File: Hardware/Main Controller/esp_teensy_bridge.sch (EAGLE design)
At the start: 64 parts, among them IC1 BQ79600PWRQ1, Q5 VISHAY_SIS862DN-T1-GE3VISHAY_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, Q6 VISHAY_SIS862DN-T1-GE3VISHAY_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, Q7 VISHAY_SIS862DN-T1-GE3VISHAY_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, Q8 VISHAY_SIS862DN-T1-GE3VISHAY_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, U1 MCP2562-E/SN, X1 5566-12

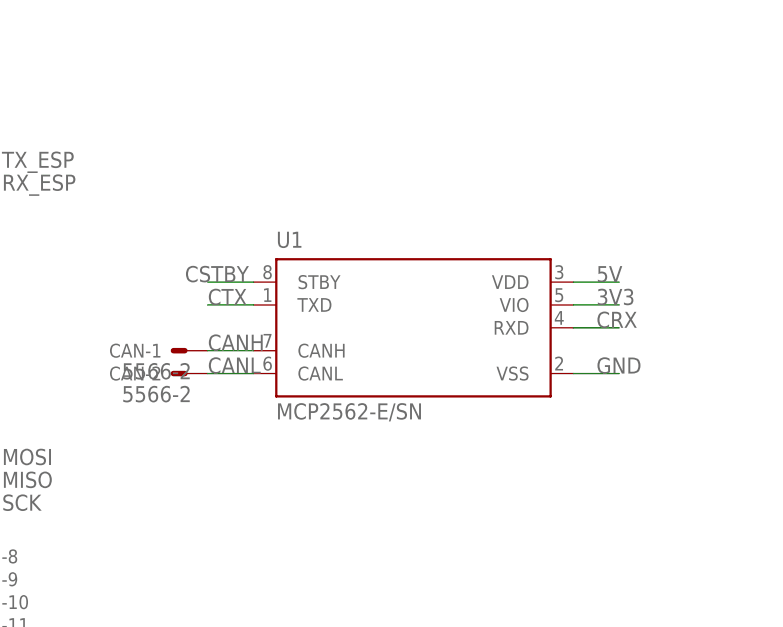
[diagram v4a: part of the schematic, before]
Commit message: Work on BQ library, RC fix for SR
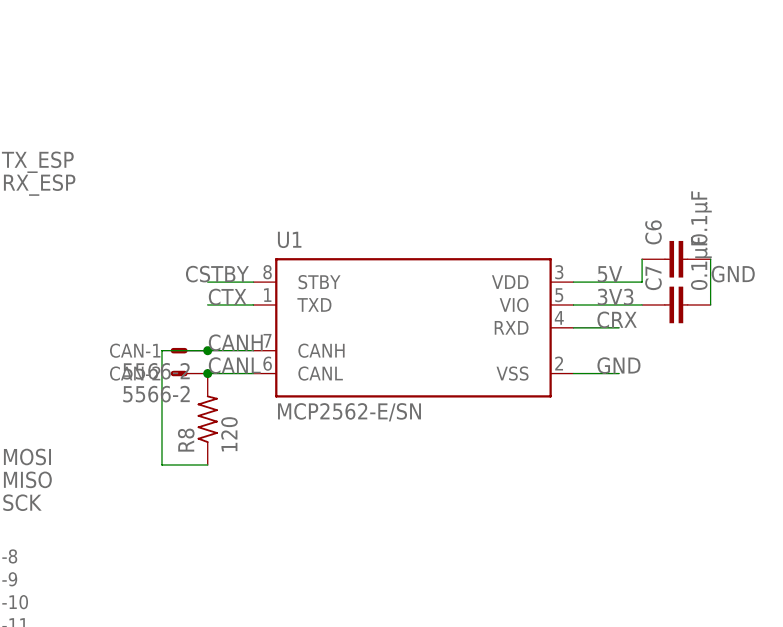
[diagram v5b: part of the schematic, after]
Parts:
- added C6, C7: 0.1μF, rcl:C-EUC0603
- added R8: 120, rcl:R-US_R0603
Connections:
- net 3V3: now also C7.1
- net 5V: now also C6.1
- net CANH: now also R8.1
- net CANL: now also R8.2
- net GND: now also C6.2, C7.2
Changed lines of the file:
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@@
 <part name="U1" library="MCP2562-E_SN" deviceset="MCP2562-E/SN" device=""/>
 <part name="CAN" library="con-molex" library_urn="urn:adsk.eagle:library:165" deviceset="5566-2" device="" package3d_urn="urn:adsk.eagle:package:8078583/1"/>
+<part name="C6" library="rcl" library_urn="urn:adsk.eagle:library:334" deviceset="C-EU" device="C0603" package3d_urn="urn:adsk.eagle:package:23616/2" value="0.1μF"/>
+<part name="C7" library="rcl" library_urn="urn:adsk.eagle:library:334" deviceset="C-EU" device="C0603" package3d_urn="urn:adsk.eagle:package:23616/2" value="0.1μF"/>
+<part name="R8" library="rcl" library_urn="urn:adsk.eagle:library:334" deviceset="R-US_" device="R0603" package3d_urn="urn:adsk.eagle:package:23555/3" value="120"/>
 </parts>
 <sheets>
@@
 <attribute name="NAME" x="124.46" y="79.502" size="1.524" layer="95" rot="R180"/>
 <attribute name="VALUE" x="127.762" y="77.343" size="1.778" layer="96" rot="R180"/>
+</instance>
+<instance part="C6" gate="G$1" x="180.34" y="91.44" smashed="yes" rot="R90">
+<attribute name="NAME" x="179.959" y="92.964" size="1.778" layer="95" rot="R90"/>
+<attribute name="VALUE" x="185.039" y="92.964" size="1.778" layer="96" rot="R90"/>
+</instance>
+<instance part="C7" gate="G$1" x="180.34" y="86.36" smashed="yes" rot="R90">
+<attribute name="NAME" x="179.959" y="87.884" size="1.778" layer="95" rot="R90"/>
+<attribute name="VALUE" x="185.039" y="87.884" size="1.778" layer="96" rot="R90"/>
+</instance>
+<instance part="R8" gate="G$1" x="129.54" y="73.66" smashed="yes" rot="R90">
+<attribute name="NAME" x="128.0414" y="69.85" size="1.778" layer="95" rot="R90"/>
+<attribute name="VALUE" x="132.842" y="69.85" size="1.778" layer="96" rot="R90"/>
 </instance>
 </instances>
@@
 <label x="172.72" y="78.74" size="1.778" layer="95"/>
 </segment>
+<segment>
+<pinref part="C6" gate="G$1" pin="2"/>
+<pinref part="C7" gate="G$1" pin="2"/>
+<wire x1="185.42" y1="91.44" x2="185.42" y2="86.36" width="0.1524" layer="91"/>
+<label x="185.42" y="88.9" size="1.778" layer="95"/>
+</segment>
 </net>
 <net name="N$1" class="0">
@@
 <segment>
 <pinref part="U1" gate="G$1" pin="VDD"/>
-<wire x1="170.18" y1="88.9" x2="175.26" y2="88.9" width="0.1524" layer="91"/>
+<wire x1="170.18" y1="88.9" x2="177.8" y2="88.9" width="0.1524" layer="91"/>
 <label x="172.72" y="88.9" size="1.778" layer="95"/>
+<pinref part="C6" gate="G$1" pin="1"/>
+<wire x1="177.8" y1="88.9" x2="177.8" y2="91.44" width="0.1524" layer="91"/>
 </segment>
 </net>
@@
 <segment>
 <pinref part="U1" gate="G$1" pin="VIO"/>
-<wire x1="170.18" y1="86.36" x2="175.26" y2="86.36" width="0.1524" layer="91"/>
+<wire x1="170.18" y1="86.36" x2="177.8" y2="86.36" width="0.1524" layer="91"/>
 <label x="172.72" y="86.36" size="1.778" layer="95"/>
+<pinref part="C7" gate="G$1" pin="1"/>
 </segment>
 </net>
@@
 <wire x1="134.62" y1="81.28" x2="129.54" y2="81.28" width="0.1524" layer="91"/>
 <label x="129.54" y="81.28" size="1.778" layer="95"/>
+<wire x1="129.54" y1="81.28" x2="124.46" y2="81.28" width="0.1524" layer="91"/>
+<wire x1="124.46" y1="81.28" x2="124.46" y2="68.58" width="0.1524" layer="91"/>
+<junction x="129.54" y="81.28"/>
+<pinref part="R8" gate="G$1" pin="1"/>
+<wire x1="124.46" y1="68.58" x2="129.54" y2="68.58" width="0.1524" layer="91"/>
 </segment>
 </net>
@@
 <wire x1="134.62" y1="78.74" x2="129.54" y2="78.74" width="0.1524" layer="91"/>
 <label x="129.54" y="78.74" size="1.778" layer="95"/>
-</segment>
-</net>
+<pinref part="R8" gate="G$1" pin="2"/>
+<junction x="129.54" y="78.74"/>
+</segment>
+</net>

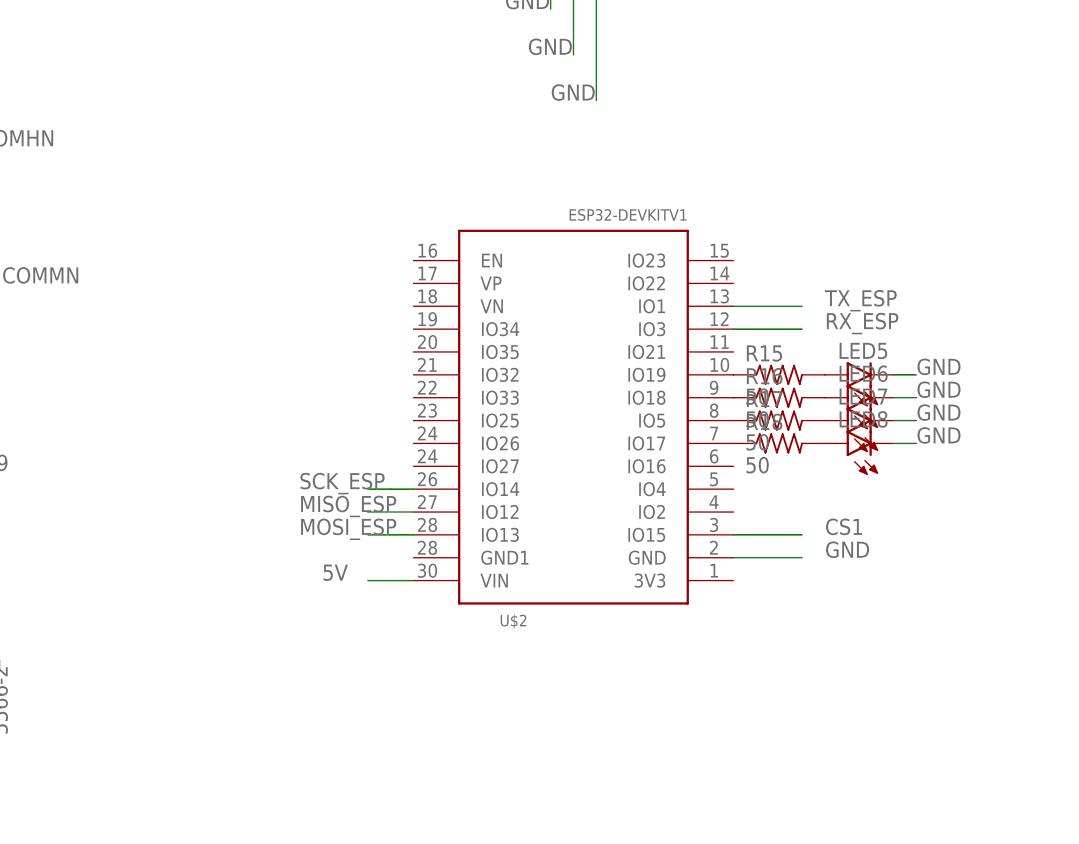
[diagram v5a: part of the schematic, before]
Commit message: ESP32-devkitc-32D instead ov DEVKIT V1
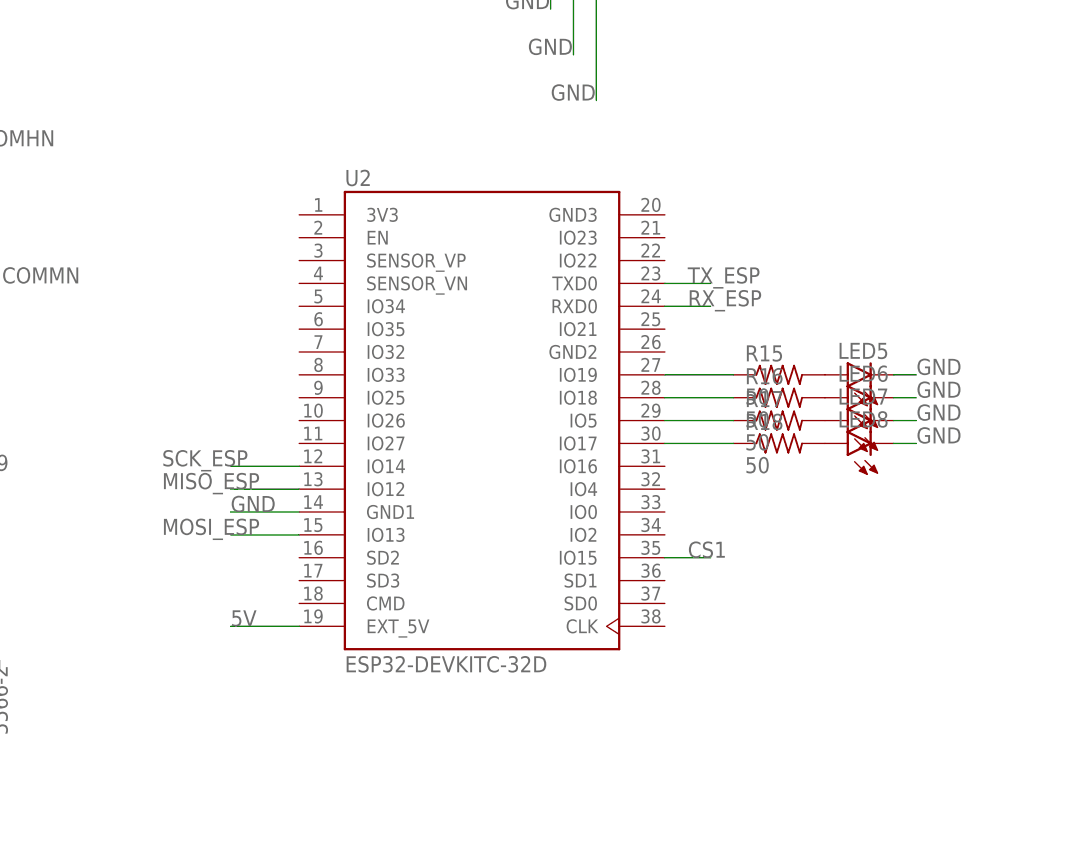
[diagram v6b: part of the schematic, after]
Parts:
- removed U$2: ESP32DEVKITV1, ESP32-DEVKITV1:ESP32DEVKITV1
- added U2: ESP32-DEVKITC-32D, ESP32-DEVKITC-32D:ESP32-DEVKITC-32D
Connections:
- net 5V: now also U2.EXT_5V; no longer U$2.VIN
- net CS1: now also U2.IO15; no longer U$2.IO15
- net GND: now also U2.GND1; no longer U$2.GND
- net MISO_ESP: now also U2.IO12; no longer U$2.IO12
- net MOSI_ESP: now also U2.IO13; no longer U$2.IO13
- net N$28: now also U2.IO19; no longer U$2.IO19
- net N$29: now also U2.IO18; no longer U$2.IO18
- net N$30: now also U2.IO5; no longer U$2.IO5
- net N$31: now also U2.IO17; no longer U$2.IO17
- net RX_ESP: now also U2.RXD0; no longer U$2.IO3
- net SCK_ESP: now also U2.IO14; no longer U$2.IO14
- net TX_ESP: now also U2.TXD0; no longer U$2.IO1
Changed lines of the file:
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@@
 <parts>
 <part name="IC1" library="BQ79600" deviceset="BQ79600PWRQ1" device=""/>
-<part name="U$2" library="ESP32-DEVKITV1" deviceset="ESP32DEVKITV1" device=""/>
 <part name="C1" library="rcl" library_urn="urn:adsk.eagle:library:334" deviceset="C-EU" device="C0603" package3d_urn="urn:adsk.eagle:package:23616/2" value="0.22μF"/>
 <part name="C2" library="rcl" library_urn="urn:adsk.eagle:library:334" deviceset="C-EU" device="C0603" package3d_urn="urn:adsk.eagle:package:23616/2" value="0.1μF"/>
@@
 <part name="C7" library="rcl" library_urn="urn:adsk.eagle:library:334" deviceset="C-EU" device="C0603" package3d_urn="urn:adsk.eagle:package:23616/2" value="0.1μF"/>
 <part name="R8" library="rcl" library_urn="urn:adsk.eagle:library:334" deviceset="R-US_" device="R0603" package3d_urn="urn:adsk.eagle:package:23555/3" value="120"/>
+<part name="U2" library="ESP32-DEVKITC-32D" deviceset="ESP32-DEVKITC-32D" device=""/>
 </parts>
 <sheets>
@@
 <attribute name="VALUE" x="-19.05" y="71.12" size="1.778" layer="96" align="center-left"/>
 </instance>
-<instance part="U$2" gate="G$1" x="63.5" y="-10.16" smashed="yes" rot="R90">
-<attribute name="NAME" x="58.42" y="-36.83" size="1.27" layer="95" rot="R180"/>
-</instance>
 <instance part="C1" gate="G$1" x="-68.58" y="66.04" smashed="yes" rot="R270">
 <attribute name="NAME" x="-68.199" y="64.516" size="1.778" layer="95" rot="R270"/>
@@
 <attribute name="NAME" x="128.0414" y="69.85" size="1.778" layer="95" rot="R90"/>
 <attribute name="VALUE" x="132.842" y="69.85" size="1.778" layer="96" rot="R90"/>
+</instance>
+<instance part="U2" gate="G$1" x="53.34" y="-15.24" smashed="yes">
+<attribute name="NAME" x="38.0828" y="10.8243" size="1.78" layer="95"/>
+<attribute name="VALUE" x="38.0837" y="-43.2098" size="1.7799" layer="96"/>
 </instance>
 </instances>
@@
 <wire x1="-15.24" y1="48.26" x2="-10.16" y2="48.26" width="0.1524" layer="91"/>
 <label x="-7.62" y="48.26" size="1.778" layer="95"/>
-</segment>
-<segment>
-<pinref part="U$2" gate="G$1" pin="GND"/>
-<wire x1="81.28" y1="-30.48" x2="88.9" y2="-30.48" width="0.1524" layer="91"/>
-<label x="91.44" y="-30.48" size="1.778" layer="95"/>
 </segment>
 <segment>
@@
 <label x="185.42" y="88.9" size="1.778" layer="95"/>
 </segment>
+<segment>
+<pinref part="U2" gate="G$1" pin="GND1"/>
+<wire x1="33.02" y1="-25.4" x2="25.4" y2="-25.4" width="0.1524" layer="91"/>
+<label x="25.4" y="-25.4" size="1.778" layer="95"/>
+</segment>
 </net>
 <net name="N$1" class="0">
@@
 </segment>
 <segment>
-<pinref part="U$2" gate="G$1" pin="IO1"/>
-<wire x1="81.28" y1="-2.54" x2="88.9" y2="-2.54" width="0.1524" layer="91"/>
-<label x="91.44" y="-2.54" size="1.778" layer="95"/>
+<pinref part="U2" gate="G$1" pin="TXD0"/>
+<wire x1="73.66" y1="0" x2="78.74" y2="0" width="0.1524" layer="91"/>
+<label x="76.2" y="0" size="1.778" layer="95"/>
 </segment>
 </net>
@@
 </segment>
 <segment>
-<pinref part="U$2" gate="G$1" pin="IO3"/>
-<wire x1="81.28" y1="-5.08" x2="88.9" y2="-5.08" width="0.1524" layer="91"/>
-<label x="91.44" y="-5.08" size="1.778" layer="95"/>
+<pinref part="U2" gate="G$1" pin="RXD0"/>
+<wire x1="73.66" y1="-2.54" x2="78.74" y2="-2.54" width="0.1524" layer="91"/>
+<label x="76.2" y="-2.54" size="1.778" layer="95"/>
 </segment>
 </net>
 <net name="5V" class="0">
-<segment>
-<pinref part="U$2" gate="G$1" pin="VIN"/>
-<wire x1="45.72" y1="-33.02" x2="40.64" y2="-33.02" width="0.1524" layer="91"/>
-<label x="35.56" y="-33.02" size="1.778" layer="95"/>
-</segment>
 <segment>
 <pinref part="TME1205S" gate="G$1" pin="+VOUT"/>
@@
 <pinref part="C6" gate="G$1" pin="1"/>
 <wire x1="177.8" y1="88.9" x2="177.8" y2="91.44" width="0.1524" layer="91"/>
+</segment>
+<segment>
+<pinref part="U2" gate="G$1" pin="EXT_5V"/>
+<wire x1="33.02" y1="-38.1" x2="25.4" y2="-38.1" width="0.1524" layer="91"/>
+<label x="25.4" y="-38.1" size="1.778" layer="95"/>
 </segment>
 </net>
@@
 </segment>
 <segment>
-<pinref part="U$2" gate="G$1" pin="IO15"/>
-<wire x1="81.28" y1="-27.94" x2="88.9" y2="-27.94" width="0.1524" layer="91"/>
-<label x="91.44" y="-27.94" size="1.778" layer="95"/>
+<pinref part="U2" gate="G$1" pin="IO15"/>
+<wire x1="73.66" y1="-30.48" x2="78.74" y2="-30.48" width="0.1524" layer="91"/>
+<label x="76.2" y="-30.48" size="1.778" layer="95"/>
 </segment>
 </net>
@@
 </segment>
 <segment>
-<pinref part="U$2" gate="G$1" pin="IO13"/>
-<wire x1="45.72" y1="-27.94" x2="40.64" y2="-27.94" width="0.1524" layer="91"/>
-<label x="33.02" y="-27.94" size="1.778" layer="95"/>
+<pinref part="U2" gate="G$1" pin="IO13"/>
+<wire x1="33.02" y1="-27.94" x2="25.4" y2="-27.94" width="0.1524" layer="91"/>
+<label x="17.78" y="-27.94" size="1.778" layer="95"/>
 </segment>
 </net>
@@
 </segment>
 <segment>
-<pinref part="U$2" gate="G$1" pin="IO12"/>
-<wire x1="45.72" y1="-25.4" x2="40.64" y2="-25.4" width="0.1524" layer="91"/>
-<label x="33.02" y="-25.4" size="1.778" layer="95"/>
+<pinref part="U2" gate="G$1" pin="IO12"/>
+<wire x1="33.02" y1="-22.86" x2="25.4" y2="-22.86" width="0.1524" layer="91"/>
+<label x="17.78" y="-22.86" size="1.778" layer="95"/>
 </segment>
 </net>
@@
 </segment>
 <segment>
-<pinref part="U$2" gate="G$1" pin="IO14"/>
-<wire x1="45.72" y1="-22.86" x2="43.18" y2="-22.86" width="0.1524" layer="91"/>
-<wire x1="40.64" y1="-22.86" x2="43.18" y2="-22.86" width="0.1524" layer="91"/>
-<label x="33.02" y="-22.86" size="1.778" layer="95"/>
+<pinref part="U2" gate="G$1" pin="IO14"/>
+<wire x1="33.02" y1="-20.32" x2="25.4" y2="-20.32" width="0.1524" layer="91"/>
+<label x="17.78" y="-20.32" size="1.778" layer="95"/>
 </segment>
 </net>
@@
 <net name="N$28" class="0">
 <segment>
-<pinref part="U$2" gate="G$1" pin="IO19"/>
 <pinref part="R15" gate="G$1" pin="1"/>
+<wire x1="73.66" y1="-10.16" x2="81.28" y2="-10.16" width="0.1524" layer="91"/>
+<pinref part="U2" gate="G$1" pin="IO19"/>
 </segment>
 </net>
 <net name="N$29" class="0">
 <segment>
-<pinref part="U$2" gate="G$1" pin="IO18"/>
 <pinref part="R16" gate="G$1" pin="1"/>
+<wire x1="73.66" y1="-12.7" x2="81.28" y2="-12.7" width="0.1524" layer="91"/>
+<pinref part="U2" gate="G$1" pin="IO18"/>
 </segment>
 </net>
 <net name="N$30" class="0">
 <segment>
-<pinref part="U$2" gate="G$1" pin="IO5"/>
 <pinref part="R17" gate="G$1" pin="1"/>
+<wire x1="73.66" y1="-15.24" x2="81.28" y2="-15.24" width="0.1524" layer="91"/>
+<pinref part="U2" gate="G$1" pin="IO5"/>
 </segment>
 </net>
 <net name="N$31" class="0">
 <segment>
-<pinref part="U$2" gate="G$1" pin="IO17"/>
 <pinref part="R18" gate="G$1" pin="1"/>
-</segment>
-</net>
+<wire x1="73.66" y1="-17.78" x2="81.28" y2="-17.78" width="0.1524" layer="91"/>
+<pinref part="U2" gate="G$1" pin="IO17"/>
+</segment>
+</net>
